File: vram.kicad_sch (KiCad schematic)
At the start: 2 parts, among them U6 62256

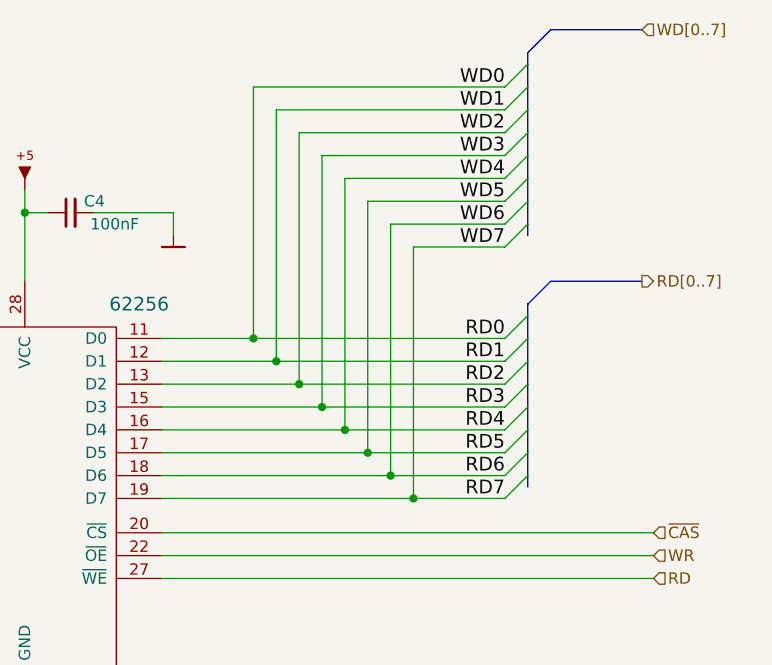
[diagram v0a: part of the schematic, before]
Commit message: Update to latest Artemisa kicadlibs
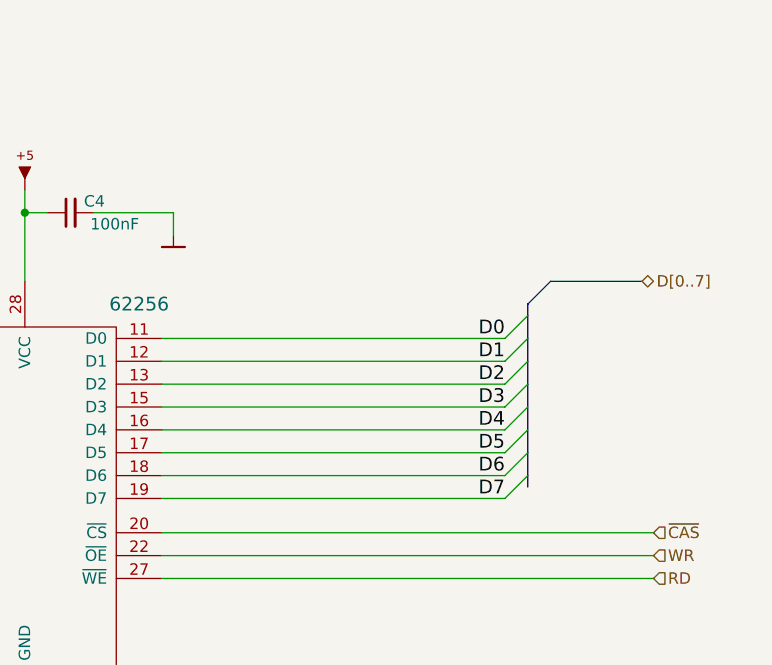
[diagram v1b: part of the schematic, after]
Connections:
- net RD0 renamed D0
- net RD1 renamed D1
- net RD2 renamed D2
- net RD3 renamed D3
- net RD4 renamed D4
- net RD5 renamed D5
- net RD6 renamed D6
- net RD7 renamed D7

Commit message: Use spare MCP6294 as CSYNC buffer
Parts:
- C4: footprint artemisa:Disc_capacitor -> PCM_artemisa:Disc_capacitor
- U6: footprint artemisa:DIP-28_600 -> PCM_artemisa:DIP-28_600
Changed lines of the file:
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@@
 			)
 		)
-		(property "Footprint" "artemisa:DIP-28_600"
+		(property "Footprint" "PCM_artemisa:DIP-28_600"
 			(at 134.62 100.33 0)
 			(hide yes)
@@
 			)
 		)
-		(property "Footprint" "artemisa:Disc_capacitor"
+		(property "Footprint" "PCM_artemisa:Disc_capacitor"
 			(at 139.7 63.5 0)
 			(hide yes)
